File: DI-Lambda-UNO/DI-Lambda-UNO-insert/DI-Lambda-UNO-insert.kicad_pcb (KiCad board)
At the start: 2 copper layers, 27 x 18 mm, 2 parts, among them J1 CONN_02X04, J2 CONN_02X04

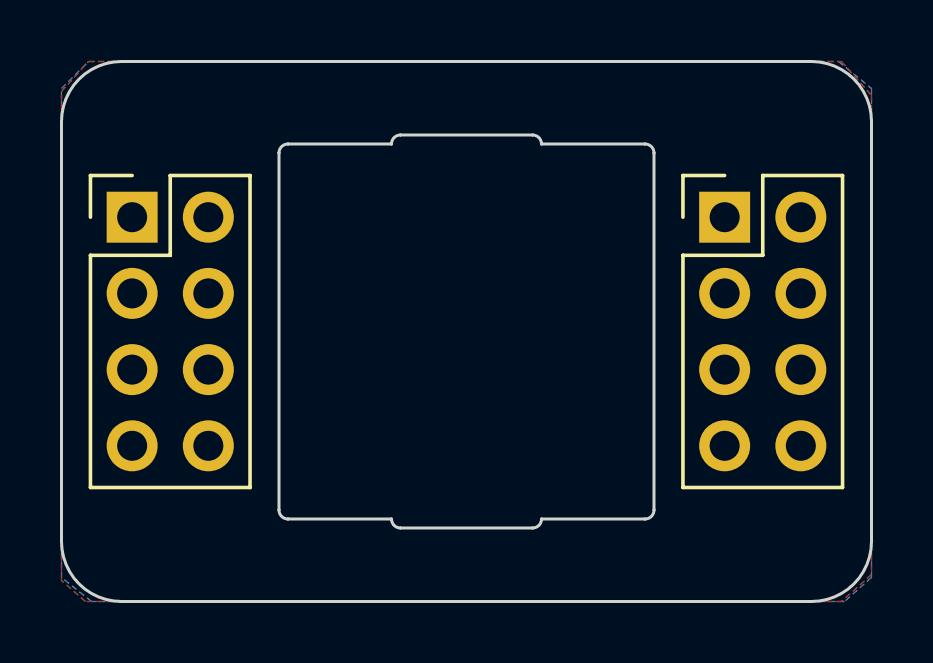
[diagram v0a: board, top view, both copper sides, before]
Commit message: Increase cuvette holder hole size to 13mm
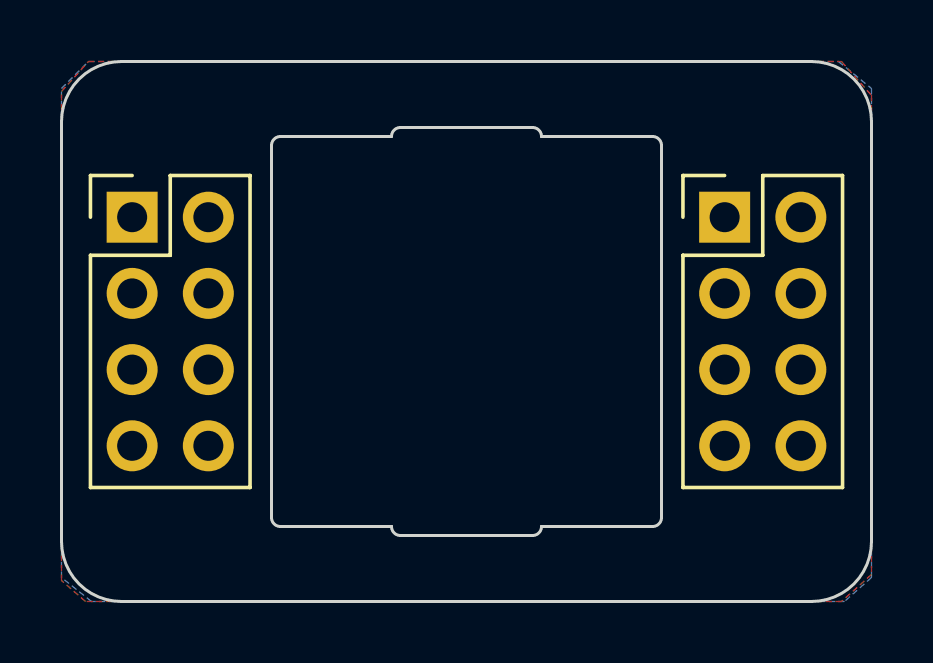
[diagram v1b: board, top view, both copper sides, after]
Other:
- outline, holes or cut-outs redrawn
- board text added: "DI-Lambda UNO v1.1"
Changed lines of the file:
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@@
-(kicad_pcb (version 20170123) (host pcbnew "(2017-07-27 revision 3ee2f80)-test1")
+(kicad_pcb (version 20170123) (host pcbnew "(2017-09-07 revision 3b08636)-master")
   (general
     (thickness 1.6)
-    (drawings 26)
+    (drawings 31)
     (tracks 0)
     (zones 0)
@@
     (last_trace_width 0.25)
     (trace_clearance 0.2)
-    (zone_clearance 0.3)
+    (zone_clearance 0.25)
     (zone_45_only yes)
     (trace_min 0.2)
@@
       (layerselection 0x000f0_ffffffff)
       (usegerberextensions true)
+      (usegerberattributes true)
+      (usegerberadvancedattributes true)
+      (creategerberjobfile true)
       (excludeedgelayer false)
       (linewidth 0.100000)
@@
     )
   )
+  (gr_text "DI-Lambda UNO v1.1" (at 158.705 50.42) (layer B.Mask)
+    (effects (font (size 1 1) (thickness 0.2)) (justify mirror))
+  )
+  (dimension 2.2 (width 0.3) (layer Eco1.User)
+    (gr_text "2.200 mm" (at 163.005 50.37 90) (layer Eco1.User)
+      (effects (font (size 1.5 1.5) (thickness 0.3)))
+    )
+    (feature1 (pts (xy 160.505 49.27) (xy 164.355 49.27)))
+    (feature2 (pts (xy 160.505 51.47) (xy 164.355 51.47)))
+    (crossbar (pts (xy 161.655 51.47) (xy 161.655 49.27)))
+    (arrow1a (pts (xy 161.655 49.27) (xy 162.241421 50.396504)))
+    (arrow1b (pts (xy 161.655 49.27) (xy 161.068579 50.396504)))
+    (arrow2a (pts (xy 161.655 51.47) (xy 162.241421 50.343496)))
+    (arrow2b (pts (xy 161.655 51.47) (xy 161.068579 50.343496)))
+  )
+  (dimension 2.2 (width 0.3) (layer Eco1.User)
+    (gr_text "2.200 mm" (at 164.005 66.17 270) (layer Eco1.User)
+      (effects (font (size 1.5 1.5) (thickness 0.3)))
+    )
+    (feature1 (pts (xy 160.105 67.27) (xy 165.355 67.27)))
+    (feature2 (pts (xy 160.105 65.07) (xy 165.355 65.07)))
+    (crossbar (pts (xy 162.655 65.07) (xy 162.655 67.27)))
+    (arrow1a (pts (xy 162.655 67.27) (xy 162.068579 66.143496)))
+    (arrow1b (pts (xy 162.655 67.27) (xy 163.241421 66.143496)))
+    (arrow2a (pts (xy 162.655 65.07) (xy 162.068579 66.196504)))
+    (arrow2b (pts (xy 162.655 65.07) (xy 163.241421 66.196504)))
+  )
+  (dimension 13 (width 0.3) (layer Eco1.User)
+    (gr_text "13.000 mm" (at 167.355 58.27 270) (layer Eco1.User)
+      (effects (font (size 1.5 1.5) (thickness 0.3)))
+    )
+    (feature1 (pts (xy 164.655 64.77) (xy 168.705 64.77)))
+    (feature2 (pts (xy 164.655 51.77) (xy 168.705 51.77)))
+    (crossbar (pts (xy 166.005 51.77) (xy 166.005 64.77)))
+    (arrow1a (pts (xy 166.005 64.77) (xy 165.418579 63.643496)))
+    (arrow1b (pts (xy 166.005 64.77) (xy 166.591421 63.643496)))
+    (arrow2a (pts (xy 166.005 51.77) (xy 165.418579 52.896504)))
+    (arrow2b (pts (xy 166.005 51.77) (xy 166.591421 52.896504)))
+  )
+  (dimension 13 (width 0.3) (layer Eco1.User)
+    (gr_text "13.000 mm" (at 158.605 49.72) (layer Eco1.User)
+      (effects (font (size 1.5 1.5) (thickness 0.3)))
+    )
+    (feature1 (pts (xy 165.105 52.37) (xy 165.105 48.37)))
+    (feature2 (pts (xy 152.105 52.37) (xy 152.105 48.37)))
+    (crossbar (pts (xy 152.105 51.07) (xy 165.105 51.07)))
+    (arrow1a (pts (xy 165.105 51.07) (xy 163.978496 51.656421)))
+    (arrow1b (pts (xy 165.105 51.07) (xy 163.978496 50.483579)))
+    (arrow2a (pts (xy 152.105 51.07) (xy 153.231504 51.656421)))
+    (arrow2b (pts (xy 152.105 51.07) (xy 153.231504 50.483579)))
+  )
   (dimension 18 (width 0.3) (layer Eco1.User)
-    (gr_text "18.000 mm" (at 177.255 58.27 270) (layer Eco1.User)
-      (effects (font (size 1.5 1.5) (thickness 0.3)))
-    )
-    (feature1 (pts (xy 172.105 67.27) (xy 178.605 67.27)))
-    (feature2 (pts (xy 172.105 49.27) (xy 178.605 49.27)))
-    (crossbar (pts (xy 175.905 49.27) (xy 175.905 67.27)))
-    (arrow1a (pts (xy 175.905 67.27) (xy 175.318579 66.143496)))
-    (arrow1b (pts (xy 175.905 67.27) (xy 176.491421 66.143496)))
-    (arrow2a (pts (xy 175.905 49.27) (xy 175.318579 50.396504)))
-    (arrow2b (pts (xy 175.905 49.27) (xy 176.491421 50.396504)))
+    (gr_text "18.000 mm" (at 175.205 58.27 270) (layer Eco1.User)
+      (effects (font (size 1.5 1.5) (thickness 0.3)))
+    )
+    (feature1 (pts (xy 170.055 67.27) (xy 176.555 67.27)))
+    (feature2 (pts (xy 170.055 49.27) (xy 176.555 49.27)))
+    (crossbar (pts (xy 173.855 49.27) (xy 173.855 67.27)))
+    (arrow1a (pts (xy 173.855 67.27) (xy 173.268579 66.143496)))
+    (arrow1b (pts (xy 173.855 67.27) (xy 174.441421 66.143496)))
+    (arrow2a (pts (xy 173.855 49.27) (xy 173.268579 50.396504)))
+    (arrow2b (pts (xy 173.855 49.27) (xy 174.441421 50.396504)))
   )
   (dimension 27 (width 0.3) (layer Eco1.User)
@@
   (gr_arc (start 170.105 51.27) (end 170.105 49.27) (angle 90) (layer Edge.Cuts) (width 0.1))
   (gr_arc (start 147.105 51.27) (end 145.105 51.27) (angle 90) (layer Edge.Cuts) (width 0.1))
-  (gr_arc (start 152.655 52.32) (end 152.355 52.32) (angle 90) (layer Edge.Cuts) (width 0.1))
-  (gr_arc (start 164.555 52.32) (end 164.555 52.02) (angle 90) (layer Edge.Cuts) (width 0.1))
-  (gr_arc (start 164.555 64.22) (end 164.855 64.22) (angle 90) (layer Edge.Cuts) (width 0.1))
-  (gr_arc (start 152.655 64.22) (end 152.655 64.52) (angle 90) (layer Edge.Cuts) (width 0.1))
-  (gr_arc (start 160.805 64.52) (end 161.105 64.52) (angle 90) (layer Edge.Cuts) (width 0.1))
-  (gr_arc (start 156.405 64.52) (end 156.405 64.82) (angle 90) (layer Edge.Cuts) (width 0.1))
-  (gr_arc (start 160.805 52.02) (end 160.805 51.72) (angle 90) (layer Edge.Cuts) (width 0.1))
-  (gr_arc (start 156.405 52.02) (end 156.105 52.02) (angle 90) (layer Edge.Cuts) (width 0.1))
-  (gr_line (start 152.355 52.32) (end 152.355 64.22) (layer Edge.Cuts) (width 0.1))
+  (gr_arc (start 152.405 52.07) (end 152.105 52.07) (angle 90) (layer Edge.Cuts) (width 0.1))
+  (gr_arc (start 164.805 52.07) (end 164.805 51.77) (angle 90) (layer Edge.Cuts) (width 0.1))
+  (gr_arc (start 164.805 64.47) (end 165.105 64.47) (angle 90) (layer Edge.Cuts) (width 0.1))
+  (gr_arc (start 152.405 64.47) (end 152.405 64.77) (angle 90) (layer Edge.Cuts) (width 0.1))
+  (gr_arc (start 160.805 64.77) (end 161.105 64.77) (angle 90) (layer Edge.Cuts) (width 0.1))
+  (gr_arc (start 156.405 64.77) (end 156.405 65.07) (angle 90) (layer Edge.Cuts) (width 0.1))
+  (gr_arc (start 160.805 51.77) (end 160.805 51.47) (angle 90) (layer Edge.Cuts) (width 0.1))
+  (gr_arc (start 156.405 51.77) (end 156.105 51.77) (angle 90) (layer Edge.Cuts) (width 0.1))
+  (gr_line (start 152.105 52.07) (end 152.105 64.47) (layer Edge.Cuts) (width 0.1))
   (gr_line (start 147.105 67.27) (end 170.105 67.27) (layer Edge.Cuts) (width 0.1))
   (gr_line (start 145.105 51.27) (end 145.105 65.27) (layer Edge.Cuts) (width 0.1))
   (gr_line (start 172.105 51.27) (end 172.105 65.27) (layer Edge.Cuts) (width 0.1))
   (gr_line (start 147.105 49.27) (end 170.105 49.27) (layer Edge.Cuts) (width 0.1))
-  (gr_line (start 156.405 64.82) (end 160.805 64.82) (layer Edge.Cuts) (width 0.1))
-  (gr_line (start 156.105 52.02) (end 152.655 52.02) (layer Edge.Cuts) (width 0.1))
-  (gr_line (start 152.655 64.52) (end 156.105 64.52) (layer Edge.Cuts) (width 0.1))
-  (gr_line (start 156.405 51.72) (end 160.805 51.72) (layer Edge.Cuts) (width 0.1))
-  (gr_line (start 164.555 64.52) (end 161.105 64.52) (layer Edge.Cuts) (width 0.1))
-  (gr_line (start 164.555 52.02) (end 161.105 52.02) (layer Edge.Cuts) (width 0.1))
-  (gr_line (start 164.855 64.22) (end 164.855 52.32) (layer Edge.Cuts) (width 0.1))
+  (gr_line (start 156.405 65.07) (end 160.805 65.07) (layer Edge.Cuts) (width 0.1))
+  (gr_line (start 156.105 51.77) (end 152.405 51.77) (layer Edge.Cuts) (width 0.1))
+  (gr_line (start 152.405 64.77) (end 156.105 64.77) (layer Edge.Cuts) (width 0.1))
+  (gr_line (start 156.405 51.47) (end 160.805 51.47) (layer Edge.Cuts) (width 0.1))
+  (gr_line (start 164.805 64.77) (end 161.105 64.77) (layer Edge.Cuts) (width 0.1))
+  (gr_line (start 164.805 51.77) (end 161.105 51.77) (layer Edge.Cuts) (width 0.1))
+  (gr_line (start 165.105 64.47) (end 165.105 52.07) (layer Edge.Cuts) (width 0.1))
   (zone (net 0) (net_name "") (layer F.Cu) (hatch edge 0.508)
-    (connect_pads (clearance 0.3))
+    (connect_pads (clearance 0.25))
     (min_thickness 0.254)
     (fill yes (arc_segments 32) (thermal_gap 0.508) (thermal_bridge_width 0.508) (smoothing chamfer))
@@
     (polygon
       (pts
-        (xy 152.705 52.27) (xy 164.405 52.27) (xy 164.305 64.27) (xy 152.905 64.27)
+        (xy 152.305 51.97) (xy 164.905 51.97) (xy 164.905 64.62) (xy 152.355 64.62)
       )
     )
   )
   (zone (net 0) (net_name "") (layer B.Cu) (hatch edge 0.508)
-    (connect_pads (clearance 0.3))
+    (connect_pads (clearance 0.25))
     (min_thickness 0.254)
     (fill yes (arc_segments 16) (thermal_gap 0.508) (thermal_bridge_width 0.508))
@@
     (polygon
       (pts
-        (xy 152.764493 52.280087) (xy 164.464493 52.280087) (xy 164.405 64.27) (xy 152.605 64.27)
+        (xy 152.305 51.97) (xy 164.905 51.97) (xy 164.905 64.62) (xy 152.355 64.62)
       )
     )

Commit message: Adjust connctors on the cuvette holder
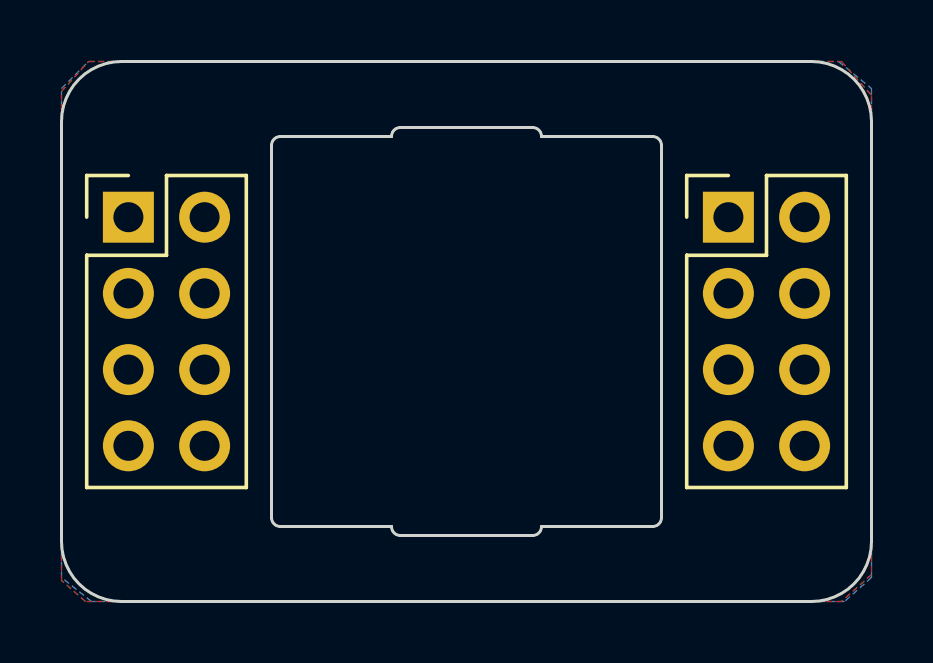
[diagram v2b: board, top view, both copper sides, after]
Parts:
- J1, J2: footprint Pin_Headers:Pin_Header_Straight_2x04_Pitch2.54mm -> Female_socket_pitch254_smt_through-board:Pin_Header_Straight_2x04_Pitch2.54mm_centered
- moved J1 4.06 mm to (168.6, 58.3)
- moved J2 3.98 mm to (148.6, 58.3)
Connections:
- J1 pad 1: Net-(J1-Pad1) -> GND
- J1 pad 2: Net-(J1-Pad2) -> GND
- J1 pad 3: Net-(J1-Pad3) -> GND
- J1 pad 4: Net-(J1-Pad4) -> GND
- J1 pad 5: Net-(J1-Pad5) -> GND
- J1 pad 6: Net-(J1-Pad6) -> GND
- J1 pad 7: Net-(J1-Pad7) -> GND
- J1 pad 8: Net-(J1-Pad8) -> GND
- J2 pad 1: Net-(J2-Pad1) -> GND
- J2 pad 2: Net-(J2-Pad2) -> GND
- J2 pad 3: Net-(J2-Pad3) -> GND
- J2 pad 4: Net-(J2-Pad4) -> GND
- J2 pad 5: Net-(J2-Pad5) -> GND
- J2 pad 6: Net-(J2-Pad6) -> GND
- J2 pad 7: Net-(J2-Pad7) -> GND
- J2 pad 8: Net-(J2-Pad8) -> GND
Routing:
- added copper zone on B.Cu, net GND
- added copper zone on F.Cu, net GND
- removed copper zone on B.Cu, net (none)
- removed copper zone on F.Cu, net (none)
